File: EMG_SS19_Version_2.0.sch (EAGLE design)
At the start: 220 parts, among them T11 OPA388, T12 OPA388, T21 OPA388, T22 OPA388

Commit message: next Version of layout 2.0: - changed position of leds, buttons and jtag connector - not every pin is routed to a connector pin - AGND,DGND on top and bottom
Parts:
- removed LED_ACT: (no value), led:LED3MM
- removed P1: (no value), con-lstb:MA05-1
- removed P2: (no value), con-lstb:MA08-1
- removed RESET: RESET, electricalmeter:PB
- added LED7: (no value), led:LEDCHIP-LED0805
- added RESET_BTN: PUSH-BUTTONSURFACE-MOUNT, Taster:PUSH-BUTTONSURFACE-MOUNT
- BTN_1, BTN_2, BTN_3, BTN_4: value (none) -> PUSH-BUTTONSURFACE-MOUNT; device electricalmeter:PB -> Taster:PUSH-BUTTONSURFACE-MOUNT
- LED1, LED2, LED3, LED4, LED5, LED6: device led:LED3MM -> led:LEDCHIP-LED0805
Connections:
- removed net N$56: P2.8, U$1.P2.0
- removed net N$78: P1.1, U$1.P1.7
- removed net N$79: P1.2, U$1.P1.6
- removed net N$80: P1.3, U$1.P1.3
- removed net N$81: P1.4, U$1.P1.1
- removed net N$82: P1.5, U$1.P1.0
- net ACT_LED: now also LED7.C, U$1.P6.6; no longer LED_ACT.C, U$1.P7.2
- net BTN1: now also BTN_1.OUT1, BTN_1.OUT2, U$1.P7.2; no longer BTN_1.S, U$1.P7.1
- net BTN2: now also BTN_2.OUT1, BTN_2.OUT2, U$1.P7.1; no longer BTN_2.S, U$1.P7.0
- net BTN3: now also BTN_3.OUT1, BTN_3.OUT2, U$1.P7.0; no longer BTN_3.S, U$1.P6.6
- net BTN4: now also BTN_4.OUT1, BTN_4.OUT2; no longer BTN_4.S
- net DGND: now also BTN_1.IN1, BTN_1.IN2, BTN_2.IN1, BTN_2.IN2, BTN_3.IN1, BTN_3.IN2, BTN_4.IN1, BTN_4.IN2, RESET_BTN.OUT1, RESET_BTN.OUT2; no longer BTN_1.P, BTN_2.P, BTN_3.P, BTN_4.P, RESET.S
- net LED1: now also LED1.C, U$1.P1.0; no longer LED3.C, U$1.P8.0
- net LED2: now also U$1.P1.1; no longer U$1.P7.6
- net LED3: now also LED3.C, U$1.P1.3; no longer LED1.C, U$1.P7.3
- net LED4: now also U$1.P2.0; no longer U$1.P7.4
- net LED5: now also U$1.P1.7; no longer U$1.P7.5
- net LED6: now also U$1.P1.6; no longer U$1.P7.7
- net N$23: now also LED1.A; no longer LED3.A
- net N$46: now also LED3.A; no longer LED1.A
- net N$47: now also LED7.A; no longer LED_ACT.A
- net N$63: no longer P2.7
- net N$64: no longer P2.6
- net N$65: no longer P2.5
- net N$66: no longer P2.4
- net N$67: no longer P2.3
- net N$68: no longer P2.2
- net N$69: no longer P2.1
- net RESET: now also RESET_BTN.IN1, RESET_BTN.IN2; no longer RESET.P
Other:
- moved on the sheet: R120, R121, R122, R123

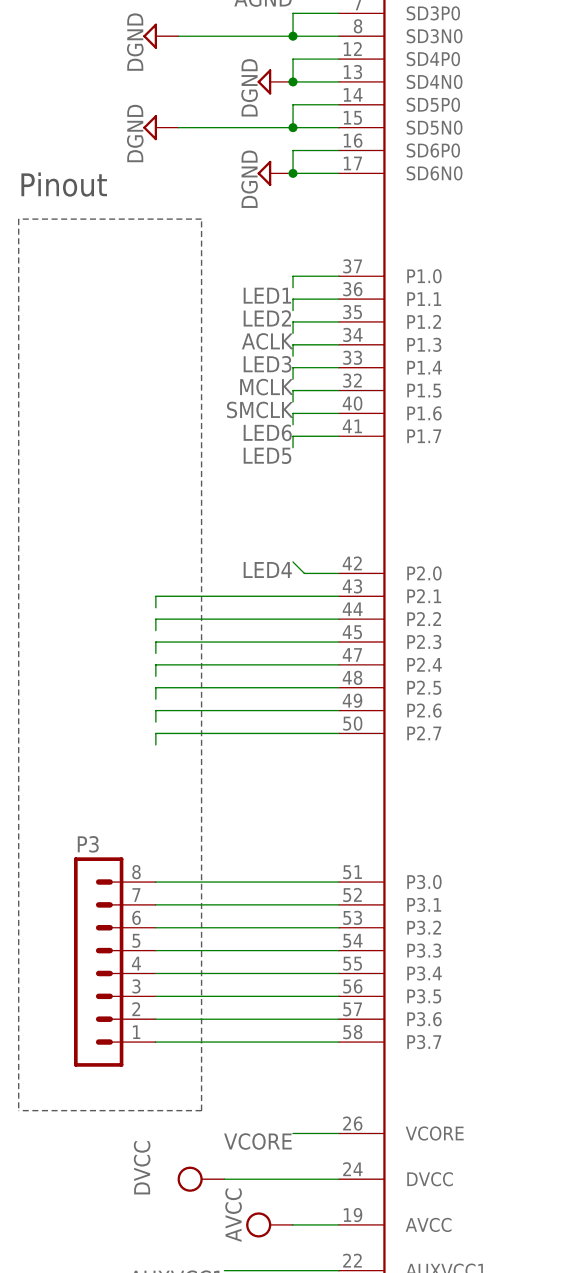
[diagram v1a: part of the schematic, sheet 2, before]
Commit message: rotated a pinout-connector
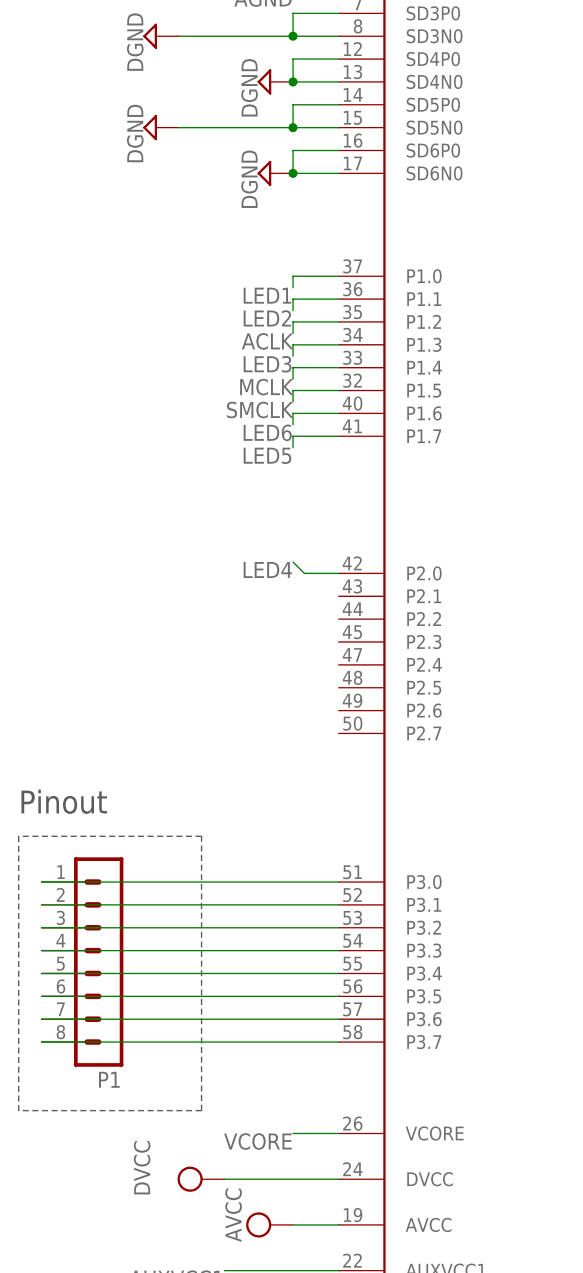
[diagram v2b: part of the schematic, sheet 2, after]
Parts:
- removed P3: (no value), con-lstb:MA08-1
- added P1: (no value), con-lstb:MA08-1
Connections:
- removed net N$63: U$1.P2.1
- removed net N$64: U$1.P2.2
- removed net N$65: U$1.P2.3
- removed net N$66: U$1.P2.4
- removed net N$67: U$1.P2.5
- removed net N$68: U$1.P2.6
- removed net N$69: U$1.P2.7
- net N$70: now also P1.1; no longer P3.8
- net N$71: now also P1.2; no longer P3.7
- net N$72: now also P1.3; no longer P3.6
- net N$73: now also P1.4; no longer P3.5
- net N$74: now also P1.5; no longer P3.4
- net N$75: now also P1.6; no longer P3.3
- net N$76: now also P1.7; no longer P3.2
- net N$77: now also P1.8; no longer P3.1
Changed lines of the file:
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@@
 <part name="SUPPLY17" library="supply2" library_urn="urn:adsk.eagle:library:372" deviceset="DGND" device=""/>
 <part name="V68" library="FE449x EVM" deviceset="AVCC" device=""/>
-<part name="P3" library="con-lstb" library_urn="urn:adsk.eagle:library:162" deviceset="MA08-1" device="" package3d_urn="urn:adsk.eagle:package:8343/1"/>
 <part name="R2" library="resistor" deviceset="R-EU_" device="R0805" value="0R"/>
 <part name="R1" library="resistor" deviceset="R-EU_" device="R0805" value="10R"/>
@@
 <part name="BTN_3" library="Taster" deviceset="PUSH-BUTTON" device="SURFACE-MOUNT"/>
 <part name="BTN_4" library="Taster" deviceset="PUSH-BUTTON" device="SURFACE-MOUNT"/>
+<part name="P1" library="con-lstb" library_urn="urn:adsk.eagle:library:162" deviceset="MA08-1" device="" package3d_urn="urn:adsk.eagle:package:8343/1"/>
 </parts>
 <sheets>
@@
 <wire x1="147.32" y1="132.08" x2="147.32" y2="213.36" width="0.1524" layer="97" style="longdash"/>
 <text x="129.54" y="215.9" size="2.54" layer="97">Pinout</text>
-<wire x1="38.1" y1="177.8" x2="17.78" y2="177.8" width="0.1524" layer="97" style="longdash"/>
-<wire x1="17.78" y1="177.8" x2="17.78" y2="78.74" width="0.1524" layer="97" style="longdash"/>
-<wire x1="38.1" y1="78.74" x2="38.1" y2="177.8" width="0.1524" layer="97" style="longdash"/>
-<text x="17.78" y="180.34" size="2.54" layer="97">Pinout</text>
+<wire x1="38.1" y1="109.22" x2="17.78" y2="109.22" width="0.1524" layer="97" style="longdash"/>
+<wire x1="17.78" y1="109.22" x2="17.78" y2="78.74" width="0.1524" layer="97" style="longdash"/>
+<wire x1="38.1" y1="78.74" x2="38.1" y2="109.22" width="0.1524" layer="97" style="longdash"/>
+<text x="17.78" y="111.76" size="2.54" layer="97">Pinout</text>
 <wire x1="152.4" y1="20.32" x2="198.12" y2="20.32" width="0.1524" layer="97" style="longdash"/>
 <wire x1="198.12" y1="20.32" x2="198.12" y2="35.56" width="0.1524" layer="97" style="longdash"/>
@@
 <attribute name="VALUE" x="42.545" y="64.135" size="1.778" layer="96" rot="R90"/>
 </instance>
-<instance part="P3" gate="1" x="25.4" y="93.98" smashed="yes">
-<attribute name="VALUE" x="24.13" y="81.28" size="1.778" layer="96"/>
-<attribute name="NAME" x="24.13" y="107.442" size="1.778" layer="95"/>
-</instance>
 <instance part="R2" gate="G$1" x="175.26" y="27.94" smashed="yes" rot="R180">
 <attribute name="NAME" x="179.07" y="26.4414" size="1.778" layer="95" rot="R180"/>
@@
 <instance part="BTN_3" gate="G$1" x="332.74" y="147.32" smashed="yes" rot="R90"/>
 <instance part="BTN_4" gate="G$1" x="355.6" y="147.32" smashed="yes" rot="R90"/>
+<instance part="P1" gate="1" x="27.94" y="96.52" smashed="yes" rot="R180">
+<attribute name="VALUE" x="29.21" y="109.22" size="1.778" layer="96" rot="R180"/>
+<attribute name="NAME" x="29.21" y="83.058" size="1.778" layer="95" rot="R180"/>
+</instance>
 </instances>
 <busses>
@@
 </segment>
 </net>
-<net name="N$63" class="0">
-<segment>
-<pinref part="U$1" gate="G$1" pin="P2.1"/>
-<wire x1="53.34" y1="135.89" x2="33.02" y2="135.89" width="0.1524" layer="91"/>
-<wire x1="33.02" y1="135.89" x2="33.02" y2="134.62" width="0.1524" layer="91"/>
-</segment>
-</net>
-<net name="N$64" class="0">
-<segment>
-<pinref part="U$1" gate="G$1" pin="P2.2"/>
-<wire x1="53.34" y1="133.35" x2="33.02" y2="133.35" width="0.1524" layer="91"/>
-<wire x1="33.02" y1="133.35" x2="33.02" y2="132.08" width="0.1524" layer="91"/>
-</segment>
-</net>
-<net name="N$65" class="0">
-<segment>
-<pinref part="U$1" gate="G$1" pin="P2.3"/>
-<wire x1="53.34" y1="130.81" x2="33.02" y2="130.81" width="0.1524" layer="91"/>
-<wire x1="33.02" y1="130.81" x2="33.02" y2="129.54" width="0.1524" layer="91"/>
-</segment>
-</net>
-<net name="N$66" class="0">
-<segment>
-<pinref part="U$1" gate="G$1" pin="P2.4"/>
-<wire x1="53.34" y1="128.27" x2="33.02" y2="128.27" width="0.1524" layer="91"/>
-<wire x1="33.02" y1="128.27" x2="33.02" y2="127" width="0.1524" layer="91"/>
-</segment>
-</net>
-<net name="N$67" class="0">
-<segment>
-<pinref part="U$1" gate="G$1" pin="P2.5"/>
-<wire x1="53.34" y1="125.73" x2="33.02" y2="125.73" width="0.1524" layer="91"/>
-<wire x1="33.02" y1="125.73" x2="33.02" y2="124.46" width="0.1524" layer="91"/>
-</segment>
-</net>
-<net name="N$68" class="0">
-<segment>
-<pinref part="U$1" gate="G$1" pin="P2.6"/>
-<wire x1="53.34" y1="123.19" x2="33.02" y2="123.19" width="0.1524" layer="91"/>
-<wire x1="33.02" y1="123.19" x2="33.02" y2="121.92" width="0.1524" layer="91"/>
-</segment>
-</net>
-<net name="N$69" class="0">
-<segment>
-<pinref part="U$1" gate="G$1" pin="P2.7"/>
-<wire x1="53.34" y1="120.65" x2="33.02" y2="120.65" width="0.1524" layer="91"/>
-<wire x1="33.02" y1="120.65" x2="33.02" y2="119.38" width="0.1524" layer="91"/>
-</segment>
-</net>
 <net name="N$70" class="0">
 <segment>
 <pinref part="U$1" gate="G$1" pin="P3.0"/>
-<pinref part="P3" gate="1" pin="8"/>
-<wire x1="53.34" y1="104.14" x2="33.02" y2="104.14" width="0.1524" layer="91"/>
+<wire x1="53.34" y1="104.14" x2="20.32" y2="104.14" width="0.1524" layer="91"/>
+<pinref part="P1" gate="1" pin="1"/>
 </segment>
 </net>
@@
 <segment>
 <pinref part="U$1" gate="G$1" pin="P3.1"/>
-<pinref part="P3" gate="1" pin="7"/>
-<wire x1="53.34" y1="101.6" x2="33.02" y2="101.6" width="0.1524" layer="91"/>
+<wire x1="53.34" y1="101.6" x2="20.32" y2="101.6" width="0.1524" layer="91"/>
+<pinref part="P1" gate="1" pin="2"/>
 </segment>
 </net>
@@
 <segment>
 <pinref part="U$1" gate="G$1" pin="P3.2"/>
-<pinref part="P3" gate="1" pin="6"/>
-<wire x1="53.34" y1="99.06" x2="33.02" y2="99.06" width="0.1524" layer="91"/>
+<wire x1="53.34" y1="99.06" x2="20.32" y2="99.06" width="0.1524" layer="91"/>
+<pinref part="P1" gate="1" pin="3"/>
 </segment>
 </net>
@@
 <segment>
 <pinref part="U$1" gate="G$1" pin="P3.3"/>
-<pinref part="P3" gate="1" pin="5"/>
-<wire x1="53.34" y1="96.52" x2="33.02" y2="96.52" width="0.1524" layer="91"/>
+<wire x1="53.34" y1="96.52" x2="20.32" y2="96.52" width="0.1524" layer="91"/>
+<pinref part="P1" gate="1" pin="4"/>
 </segment>
 </net>
@@
 <segment>
 <pinref part="U$1" gate="G$1" pin="P3.4"/>
-<pinref part="P3" gate="1" pin="4"/>
-<wire x1="53.34" y1="93.98" x2="33.02" y2="93.98" width="0.1524" layer="91"/>
+<wire x1="53.34" y1="93.98" x2="20.32" y2="93.98" width="0.1524" layer="91"/>
+<pinref part="P1" gate="1" pin="5"/>
 </segment>
 </net>
@@
 <segment>
 <pinref part="U$1" gate="G$1" pin="P3.5"/>
-<pinref part="P3" gate="1" pin="3"/>
-<wire x1="53.34" y1="91.44" x2="33.02" y2="91.44" width="0.1524" layer="91"/>
+<wire x1="53.34" y1="91.44" x2="20.32" y2="91.44" width="0.1524" layer="91"/>
+<pinref part="P1" gate="1" pin="6"/>
 </segment>
 </net>
@@
 <segment>
 <pinref part="U$1" gate="G$1" pin="P3.6"/>
-<pinref part="P3" gate="1" pin="2"/>
-<wire x1="53.34" y1="88.9" x2="33.02" y2="88.9" width="0.1524" layer="91"/>
+<wire x1="53.34" y1="88.9" x2="20.32" y2="88.9" width="0.1524" layer="91"/>
+<pinref part="P1" gate="1" pin="7"/>
 </segment>
 </net>
@@
 <segment>
 <pinref part="U$1" gate="G$1" pin="P3.7"/>
-<pinref part="P3" gate="1" pin="1"/>
-<wire x1="53.34" y1="86.36" x2="33.02" y2="86.36" width="0.1524" layer="91"/>
+<wire x1="53.34" y1="86.36" x2="20.32" y2="86.36" width="0.1524" layer="91"/>
+<pinref part="P1" gate="1" pin="8"/>
 </segment>
 </net>

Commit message: moved some wires for more GND-shielding, added labeling
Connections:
- net AGND: now also U$1.SD1N0, U$1.SD1P0, U$1.SD3N0, U$1.SD3P0, U$1.SD4N0, U$1.SD4P0, U$1.SD5N0, U$1.SD5P0, U$1.SD6N0, U$1.SD6P0
- net DGND: no longer U$1.SD1N0, U$1.SD1P0, U$1.SD3N0, U$1.SD3P0, U$1.SD4N0, U$1.SD4P0, U$1.SD5N0, U$1.SD5P0, U$1.SD6N0, U$1.SD6P0
